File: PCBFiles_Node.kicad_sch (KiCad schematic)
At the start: 1 part

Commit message: Prueba de push nro. 2
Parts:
- added R?: R_Photo, symbol Device:R_Photo
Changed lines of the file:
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@@
 (kicad_sch (version 20211123) (generator eeschema)
   (paper "A4")
+  (symbol (lib_id "Device:R_Photo") (at 104.14 90.17 0) (unit 1)
+    (in_bom yes) (on_board yes) (fields_autoplaced)
+    (property "Reference" "R?" (id 0) (at 105.918 89.2615 0)
+      (effects (font (size 1.27 1.27)) (justify left))
+    )
+    (property "Value" "R_Photo" (id 1) (at 105.918 92.0366 0)
+      (effects (font (size 1.27 1.27)) (justify left))
+    )
+    (property "Footprint" "" (id 2) (at 105.41 96.52 90)
+      (effects (font (size 1.27 1.27)) (justify left) hide)
+    )
+    (property "Datasheet" "~" (id 3) (at 104.14 91.44 0)
+      (effects (font (size 1.27 1.27)) hide)
+    )
+    (pin "1")
+    (pin "2")
+  )
   (symbol (lib_id "Device:R_Photo") (at 128.27 92.71 0) (unit 1)
     (in_bom yes) (on_board yes) (fields_autoplaced)
@@
   )
   (symbol_instances
+    (path "/692d87e9-6b70-46cc-9c78-b75193a484cc"
+      (reference "R?") (unit 1) (value "R_Photo") (footprint "")
+    )
     (path "/af347946-e3da-4427-87ab-77b747929f50"
       (reference "R?") (unit 1) (value "R_Photo") (footprint "")

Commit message: Prueba push Nro.3
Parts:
- added R?: R_Photo, symbol Device:R_Photo
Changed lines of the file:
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@@
 (kicad_sch (version 20211123) (generator eeschema)
   (paper "A4")
+  (symbol (lib_id "Device:R_Photo") (at 162.56 95.25 0) (unit 1)
+    (in_bom yes) (on_board yes) (fields_autoplaced)
+    (property "Reference" "R?" (id 0) (at 164.338 94.3415 0)
+      (effects (font (size 1.27 1.27)) (justify left))
+    )
+    (property "Value" "R_Photo" (id 1) (at 164.338 97.1166 0)
+      (effects (font (size 1.27 1.27)) (justify left))
+    )
+    (property "Footprint" "" (id 2) (at 163.83 101.6 90)
+      (effects (font (size 1.27 1.27)) (justify left) hide)
+    )
+    (property "Datasheet" "~" (id 3) (at 162.56 96.52 0)
+      (effects (font (size 1.27 1.27)) hide)
+    )
+    (pin "1")
+    (pin "2")
+  )
   (symbol (lib_id "Device:R_Photo") (at 104.14 90.17 0) (unit 1)
     (in_bom yes) (on_board yes) (fields_autoplaced)
@@
   )
   (symbol_instances
+    (path "/0fdc6f30-77bc-4e9b-8665-c8aa9acf5bf9"
+      (reference "R?") (unit 1) (value "R_Photo") (footprint "")
+    )
     (path "/692d87e9-6b70-46cc-9c78-b75193a484cc"
       (reference "R?") (unit 1) (value "R_Photo") (footprint "")

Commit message: Prueba 4
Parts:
- removed R? (x3): R_Photo, symbol Device:R_Photo
- added IC1: STM32L432KCU3, SamacSys_Parts:QFN50P500X500X60-33N-D, symbol SamacSys_Parts:STM32L432KCU3
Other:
- company: (none) -> UTEC
- title: (none) -> Diseño PCB Nodo Sensor Version 2.0
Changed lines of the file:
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@@
 (kicad_sch (version 20211123) (generator eeschema)
   (paper "A4")
-  (symbol (lib_id "Device:R_Photo") (at 162.56 95.25 0) (unit 1)
+  (title_block
+    (title "Diseño PCB Nodo Sensor Version 2.0")
+    (date "2022-09-13")
+    (company "UTEC")
+  )
+  (symbol (lib_id "SamacSys_Parts:STM32L432KCU3") (at 78.74 90.17 0) (unit 1)
     (in_bom yes) (on_board yes) (fields_autoplaced)
-    (property "Reference" "R?" (id 0) (at 164.338 94.3415 0)
-      (effects (font (size 1.27 1.27)) (justify left))
-    )
-    (property "Value" "R_Photo" (id 1) (at 164.338 97.1166 0)
-      (effects (font (size 1.27 1.27)) (justify left))
-    )
-    (property "Footprint" "" (id 2) (at 163.83 101.6 90)
+    (property "Reference" "IC1" (id 0) (at 128.0627 84.1967 0))
+    (property "Value" "STM32L432KCU3" (id 1) (at 128.0627 86.9718 0))
+    (property "Footprint" "SamacSys_Parts:QFN50P500X500X60-33N-D" (id 2) (at 120.65 72.39 0)
       (effects (font (size 1.27 1.27)) (justify left) hide)
     )
-    (property "Datasheet" "~" (id 3) (at 162.56 96.52 0)
-      (effects (font (size 1.27 1.27)) hide)
+    (property "Datasheet" "https://www.st.com/resource/en/datasheet/stm32l432kc.pdf" (id 3) (at 120.65 74.93 0)
+      (effects (font (size 1.27 1.27)) (justify left) hide)
+    )
+    (property "Description" "5.1STMICROELECTRONICS - STM32L432KCU3 - MCU, ARM CORTEX-M4, 80MHZ, UFQFPN-32" (id 4) (at 120.65 77.47 0)
+      (effects (font (size 1.27 1.27)) (justify left) hide)
+    )
+    (property "Height" "0.6" (id 5) (at 120.65 80.01 0)
+      (effects (font (size 1.27 1.27)) (justify left) hide)
+    )
+    (property "Mouser Part Number" "511-STM32L432KCU3" (id 6) (at 120.65 82.55 0)
+      (effects (font (size 1.27 1.27)) (justify left) hide)
+    )
+    (property "Mouser Price/Stock" "https://www.mouser.co.uk/ProductDetail/STMicroelectronics/STM32L432KCU3?qs=u4fy%2FsgLU9PiN2BHPc4dhw%3D%3D" (id 7) (at 120.65 85.09 0)
+      (effects (font (size 1.27 1.27)) (justify left) hide)
+    )
+    (property "Manufacturer_Name" "STMicroelectronics" (id 8) (at 120.65 87.63 0)
+      (effects (font (size 1.27 1.27)) (justify left) hide)
+    )
+    (property "Manufacturer_Part_Number" "STM32L432KCU3" (id 9) (at 120.65 90.17 0)
+      (effects (font (size 1.27 1.27)) (justify left) hide)
     )
     (pin "1")
+    (pin "10")
+    (pin "11")
+    (pin "12")
+    (pin "13")
+    (pin "14")
+    (pin "15")
+    (pin "16")
+    (pin "17")
+    (pin "18")
+    (pin "19")
     (pin "2")
-  )
-  (symbol (lib_id "Device:R_Photo") (at 104.14 90.17 0) (unit 1)
-    (in_bom yes) (on_board yes) (fields_autoplaced)
-    (property "Reference" "R?" (id 0) (at 105.918 89.2615 0)
-      (effects (font (size 1.27 1.27)) (justify left))
-    )
-    (property "Value" "R_Photo" (id 1) (at 105.918 92.0366 0)
-      (effects (font (size 1.27 1.27)) (justify left))
-    )
-    (property "Footprint" "" (id 2) (at 105.41 96.52 90)
-      (effects (font (size 1.27 1.27)) (justify left) hide)
-    )
-    (property "Datasheet" "~" (id 3) (at 104.14 91.44 0)
-      (effects (font (size 1.27 1.27)) hide)
-    )
-    (pin "1")
-    (pin "2")
-  )
-  (symbol (lib_id "Device:R_Photo") (at 128.27 92.71 0) (unit 1)
-    (in_bom yes) (on_board yes) (fields_autoplaced)
-    (property "Reference" "R?" (id 0) (at 130.048 91.8015 0)
-      (effects (font (size 1.27 1.27)) (justify left))
-    )
-    (property "Value" "R_Photo" (id 1) (at 130.048 94.5766 0)
-      (effects (font (size 1.27 1.27)) (justify left))
-    )
-    (property "Footprint" "" (id 2) (at 129.54 99.06 90)
-      (effects (font (size 1.27 1.27)) (justify left) hide)
-    )
-    (property "Datasheet" "~" (id 3) (at 128.27 93.98 0)
-      (effects (font (size 1.27 1.27)) hide)
-    )
-    (pin "1")
-    (pin "2")
+    (pin "20")
+    (pin "21")
+    (pin "22")
+    (pin "23")
+    (pin "24")
+    (pin "25")
+    (pin "26")
+    (pin "27")
+    (pin "28")
+    (pin "29")
+    (pin "3")
+    (pin "30")
+    (pin "31")
+    (pin "32")
+    (pin "33")
+    (pin "4")
+    (pin "5")
+    (pin "6")
+    (pin "7")
+    (pin "8")
+    (pin "9")
   )
   (sheet_instances
@@
   )
   (symbol_instances
-    (path "/0fdc6f30-77bc-4e9b-8665-c8aa9acf5bf9"
-      (reference "R?") (unit 1) (value "R_Photo") (footprint "")
-    )
-    (path "/692d87e9-6b70-46cc-9c78-b75193a484cc"
-      (reference "R?") (unit 1) (value "R_Photo") (footprint "")
-    )
-    (path "/af347946-e3da-4427-87ab-77b747929f50"
-      (reference "R?") (unit 1) (value "R_Photo") (footprint "")
+    (path "/2e9fa934-d7b3-41b5-86d2-0b47a3391849"
+      (reference "IC1") (unit 1) (value "STM32L432KCU3") (footprint "SamacSys_Parts:QFN50P500X500X60-33N-D")
     )
   )

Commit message: STM32 IC
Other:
- moved on the sheet: IC1
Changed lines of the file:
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@@
     (company "UTEC")
   )
-  (symbol (lib_id "SamacSys_Parts:STM32L432KCU3") (at 78.74 90.17 0) (unit 1)
+  (symbol (lib_id "SamacSys_Parts:STM32L432KCU3") (at 68.58 82.55 0) (unit 1)
     (in_bom yes) (on_board yes) (fields_autoplaced)
-    (property "Reference" "IC1" (id 0) (at 128.0627 84.1967 0))
-    (property "Value" "STM32L432KCU3" (id 1) (at 128.0627 86.9718 0))
-    (property "Footprint" "SamacSys_Parts:QFN50P500X500X60-33N-D" (id 2) (at 120.65 72.39 0)
+    (property "Reference" "IC1" (id 0) (at 91.44 93.98 0))
+    (property "Value" "STM32L432KCU3" (id 1) (at 105.41 127 0))
+    (property "Footprint" "SamacSys_Parts:QFN50P500X500X60-33N-D" (id 2) (at 123.19 72.39 0)
       (effects (font (size 1.27 1.27)) (justify left) hide)
     )
-    (property "Datasheet" "https://www.st.com/resource/en/datasheet/stm32l432kc.pdf" (id 3) (at 120.65 74.93 0)
+    (property "Datasheet" "https://www.st.com/resource/en/datasheet/stm32l432kc.pdf" (id 3) (at 123.19 74.93 0)
       (effects (font (size 1.27 1.27)) (justify left) hide)
     )
-    (property "Description" "5.1STMICROELECTRONICS - STM32L432KCU3 - MCU, ARM CORTEX-M4, 80MHZ, UFQFPN-32" (id 4) (at 120.65 77.47 0)
+    (property "Description" "5.1STMICROELECTRONICS - STM32L432KCU3 - MCU, ARM CORTEX-M4, 80MHZ, UFQFPN-32" (id 4) (at 123.19 77.47 0)
       (effects (font (size 1.27 1.27)) (justify left) hide)
     )
-    (property "Height" "0.6" (id 5) (at 120.65 80.01 0)
+    (property "Height" "0.6" (id 5) (at 123.19 69.85 0)
       (effects (font (size 1.27 1.27)) (justify left) hide)
     )
-    (property "Mouser Part Number" "511-STM32L432KCU3" (id 6) (at 120.65 82.55 0)
+    (property "Mouser Part Number" "511-STM32L432KCU3" (id 6) (at 123.19 80.01 0)
       (effects (font (size 1.27 1.27)) (justify left) hide)
     )
-    (property "Mouser Price/Stock" "https://www.mouser.co.uk/ProductDetail/STMicroelectronics/STM32L432KCU3?qs=u4fy%2FsgLU9PiN2BHPc4dhw%3D%3D" (id 7) (at 120.65 85.09 0)
+    (property "Mouser Price/Stock" "https://www.mouser.co.uk/ProductDetail/STMicroelectronics/STM32L432KCU3?qs=u4fy%2FsgLU9PiN2BHPc4dhw%3D%3D" (id 7) (at 123.19 82.55 0)
       (effects (font (size 1.27 1.27)) (justify left) hide)
     )
-    (property "Manufacturer_Name" "STMicroelectronics" (id 8) (at 120.65 87.63 0)
+    (property "Manufacturer_Name" "STMicroelectronics" (id 8) (at 123.19 85.09 0)
       (effects (font (size 1.27 1.27)) (justify left) hide)
     )
-    (property "Manufacturer_Part_Number" "STM32L432KCU3" (id 9) (at 120.65 90.17 0)
+    (property "Manufacturer_Part_Number" "STM32L432KCU3" (id 9) (at 123.19 87.63 0)
       (effects (font (size 1.27 1.27)) (justify left) hide)
     )

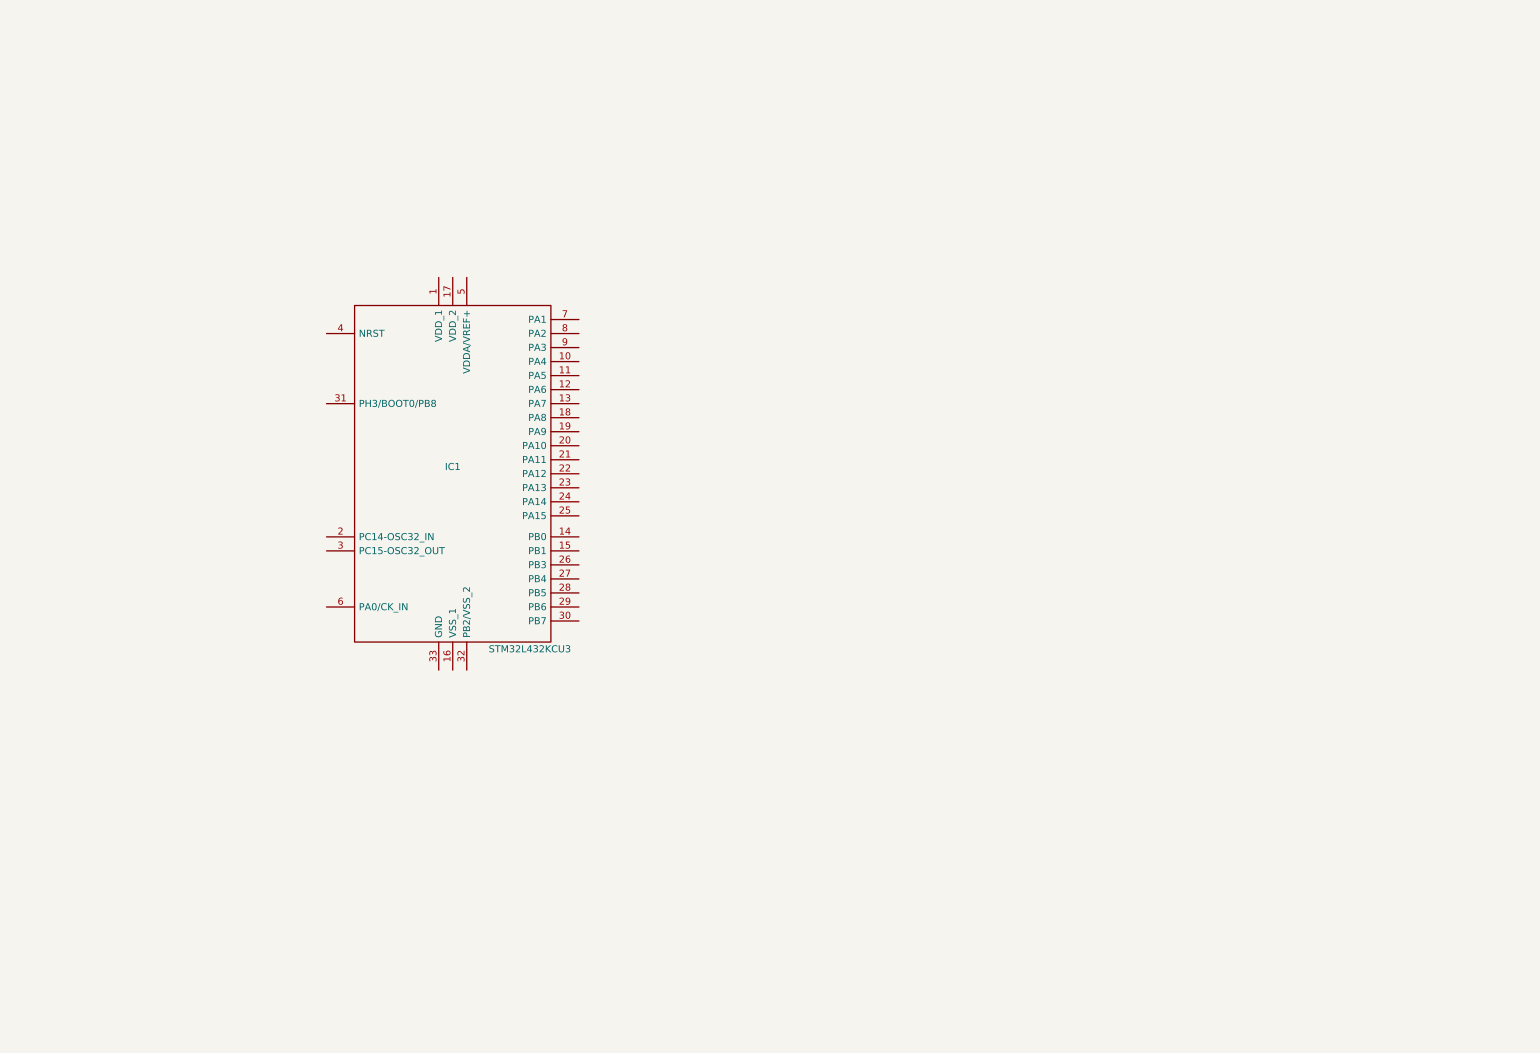
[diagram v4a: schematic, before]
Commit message: Voltage regulator, Crystal, RFM9x, base settings
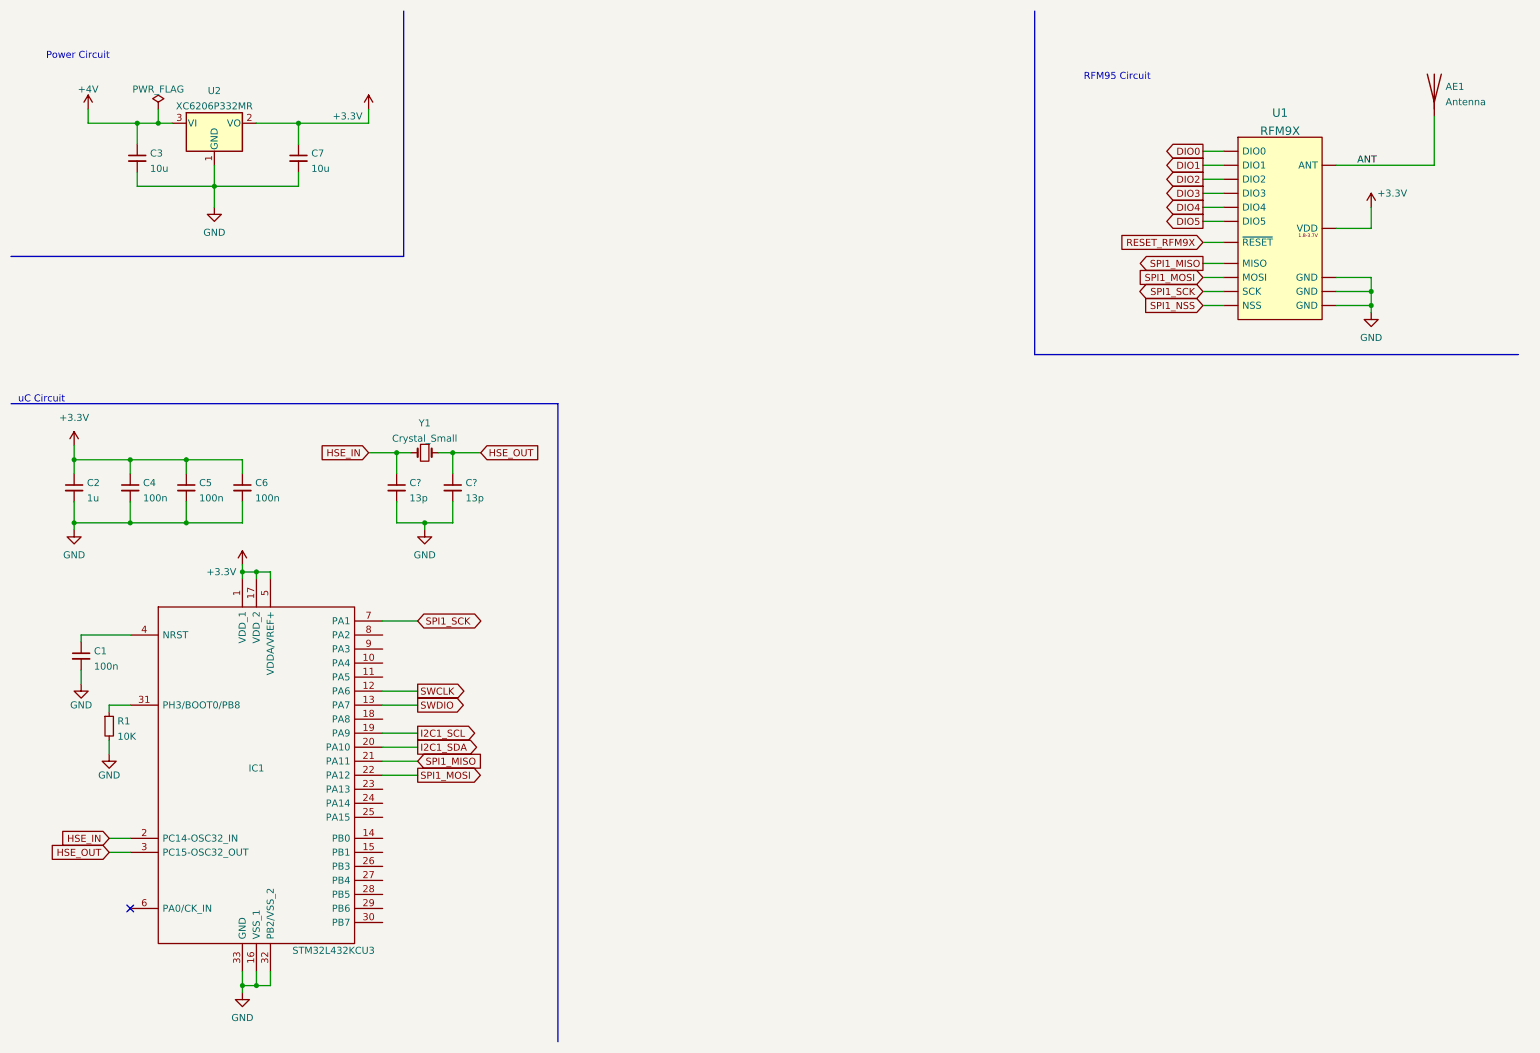
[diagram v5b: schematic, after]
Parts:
- added AE1: Antenna, symbol Device:Antenna
- added C1, C4, C5, C6: 100n, symbol Device:C_Small
- added C2: 1u, symbol Device:C_Small
- added C3, C7: 10u, symbol Device:C_Small
- added C? (x2): 13p, symbol Device:C_Small
- added R1: 10K, symbol Device:R_Small
- added U1: RFM9X, LoRa_RFM9x:RFM9X-SMD, symbol RFM9X:RFM9X
- added U2: XC6206P332MR, Package_TO_SOT_SMD:SOT-23, symbol Regulator_Linear:XC6206PxxxMR
- added Y1: Crystal_Small, symbol Device:Crystal_Small
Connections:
- net +3V3: now reaches IC1.1 (VDD_1)
- net +3V3: now also IC1.17 (VDD_2), IC1.5 (VDDA/VREF+), C2.1, C4.1, C5.1, C6.1, C7.1, U1.12 (VDD), U2.2 (VO)
- net SWCLK: now reaches IC1.12 (PA6)
- net SWDIO: now reaches IC1.13 (PA7)
- net GND: now reaches IC1.16 (VSS_1)
- net GND: now also IC1.32 (PB2/VSS_2), IC1.33 (GND), C1.2, C2.2, C3.2, C4.2, C5.2, C6.2, C7.2, C?.2, C?.2, R1.2, U1.1 (GND), U1.15 (GND), U1.8 (GND), U2.1 (GND)
- net I2C1_SCL: now reaches IC1.19 (PA9)
- net HSE_IN: now reaches IC1.2 (PC14-OSC32_IN)
- net HSE_IN: now also C?.1, Y1.2
- net I2C1_SDA: now reaches IC1.20 (PA10)
- net SPI1_MISO: now reaches IC1.21 (PA11)
- net SPI1_MISO: now also U1.2 (MISO)
- net SPI1_MOSI: now reaches IC1.22 (PA12)
- net SPI1_MOSI: now also U1.3 (MOSI)
- net HSE_OUT: now reaches IC1.3 (PC15-OSC32_OUT)
- net HSE_OUT: now also C?.1, Y1.1
- net at IC1.31 (PH3/BOOT0/PB8): now also R1.1
- net at IC1.4 (NRST): now also C1.1
- net SPI1_SCK: now reaches IC1.7 (PA1)
- net SPI1_SCK: now also U1.4 (SCK)
- new net +4V: C3.1, U2.3 (VI)
- new net ANT: AE1.1 (A), U1.16 (ANT)
- new net DIO0: U1.11 (DIO0)
- new net DIO1: U1.10 (DIO1)
- new net DIO2: U1.9 (DIO2)
- new net DIO3: U1.14 (DIO3)
- new net DIO4: U1.13 (DIO4)
- new net DIO5: U1.7 (DIO5)
- new net RESET_RFM9X: U1.6 (~{RESET})
- new net SPI1_NSS: U1.5 (NSS)
- no-connect marks 0 -> 1
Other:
- note added: "Power Circuit"
- note added: "RFM95 Circuit"
- note added: "uC Circuit"
- moved on the sheet: IC1
